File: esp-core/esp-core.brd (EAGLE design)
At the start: 35.6 x 35.6 mm, 9 parts

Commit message: core board fixes
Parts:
- removed B1: (no value), ESPstack:SKSCLDE010
- added RESET: (no value), ESPstack:SKSCLDE010
- turned R1 to 90 degrees
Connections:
- net GND: now also RESET.1, RESET.2; no longer B1.1, B1.2
- net RESET: now also RESET.3, RESET.4; no longer B1.3, B1.4
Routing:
- net EN: track 27.6 -> 23.6 mm, vias 0 -> 2
- net RESET: track 35.0 -> 37.3 mm
- net GND: track 39.6 -> 38.9 mm
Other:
- outline, holes or cut-outs redrawn

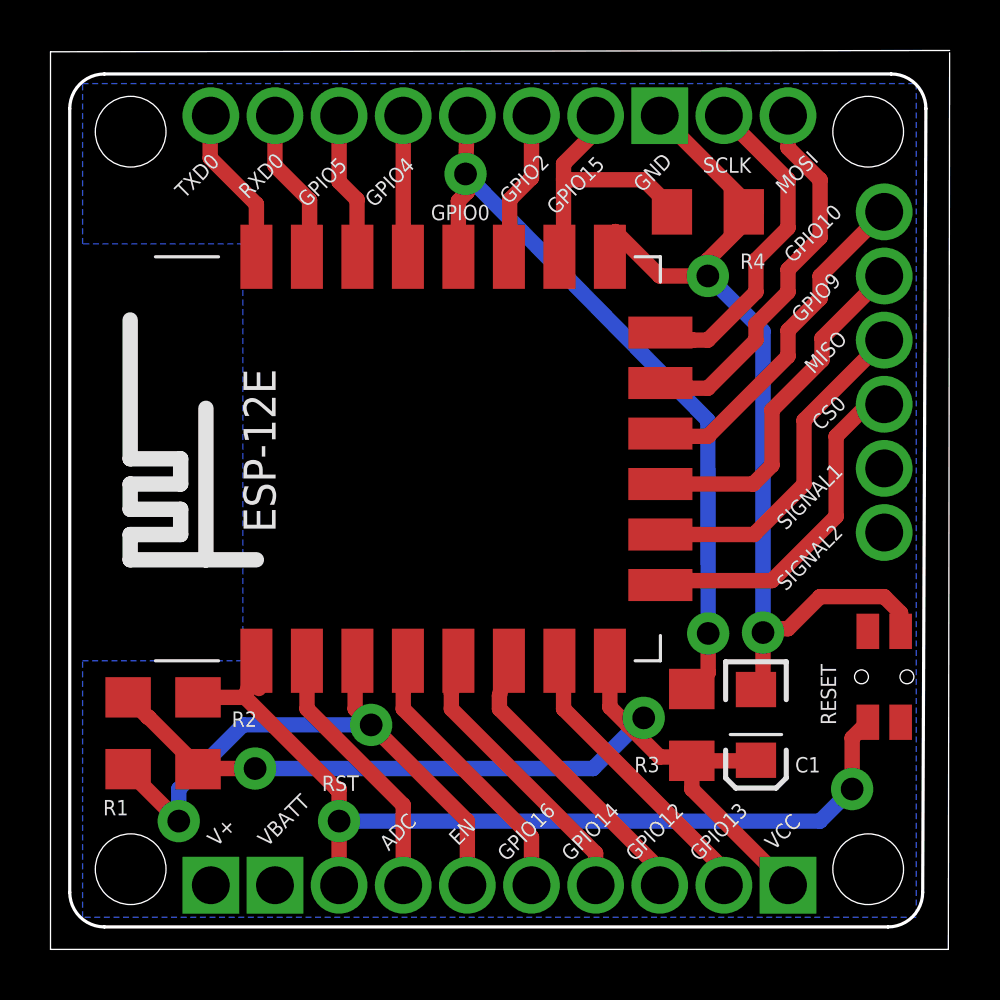
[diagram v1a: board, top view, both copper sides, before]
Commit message: Unify all boards, buttons in the same place, board dimension reduced to 1.32inch
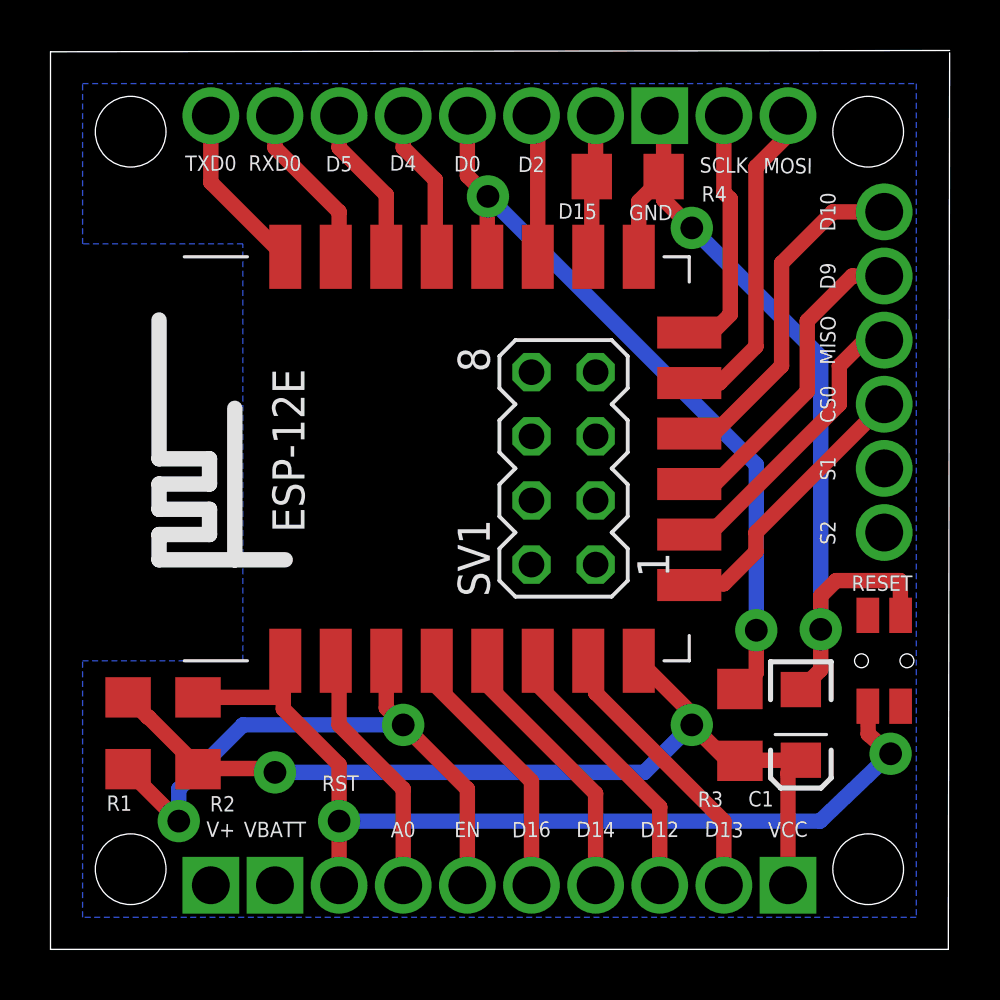
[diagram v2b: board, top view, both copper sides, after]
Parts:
- added SV1: (no value), con-lstb:MA04-2
- moved U$1 9.16 mm to (2.54, 12.7)
- moved R4 3.47 mm to (22.9, 30.6)
- moved R3 1.91 mm to (27.3, 8.89)
- moved C1 1.78 mm to (29.7, 8.89)
- moved ESP-12E 1.14 mm to (25.3, 11.4)
- moved RESET 0.63 mm to (33.0, 11.4)
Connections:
- net +3V3: now also SV1.7
- net EN: now also SV1.3
- net GND: now also SV1.2
- net GPIO0: now also SV1.6
- net GPIO2: now also SV1.4
- net RESET: now also SV1.5
- net RXD0: now also SV1.8
- net TXD0: now also SV1.1
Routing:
- net GPIO15: track 11.0 -> 5.71 mm
- net GND: track 38.9 -> 35.4 mm
- net SCLK: track 13.2 -> 9.94 mm
- net CS0: track 13.7 -> 11.1 mm
- net MOSI: track 15.1 -> 12.9 mm
- net MISO: track 13.5 -> 11.8 mm
- net GPIO9: track 14.1 -> 12.8 mm
- net RESET: track 37.3 -> 38.5 mm
- net EN: track 23.6 -> 24.3 mm
- net GPIO12: track 11.6 -> 10.9 mm
- net GPIO16: track 11.0 -> 10.5 mm
- net GPIO4: track 5.60 -> 6.14 mm
- net RXD0: track 6.16 -> 6.70 mm
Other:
- outline, holes or cut-outs redrawn
- board text added: "A0"
- board text added: "D0"
- board text added: "D10"
- board text added: "D12"
- board text added: "D13"
- board text added: "D14"
- board text added: "D15"
- board text added: "D16"
- board text added: "D2"
- board text added: "D4"
- board text added: "D5"
- board text added: "D9"
- board text added: "S1"
- board text added: "S2"
- board text added: "revision 0.2"
- board text removed: "ADC"
- board text removed: "GPIO0"
- board text removed: "GPIO10"
- board text removed: "GPIO12"
- board text removed: "GPIO13"
- board text removed: "GPIO14"
- board text removed: "GPIO15"
- board text removed: "GPIO16"
- board text removed: "GPIO2"
- board text removed: "GPIO4"
- board text removed: "GPIO5"
- board text removed: "GPIO9"
- board text removed: "SIGNAL1"
- board text removed: "SIGNAL2"
- board text removed: "prototype rev. 0.1"
